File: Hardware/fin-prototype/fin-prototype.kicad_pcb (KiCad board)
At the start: 4 copper layers, 50 x 50 mm, 80 parts, among them J1 USB_C_Receptacle_USB2.0_16P, J10 Conn_01x01_Pin, J11 Conn_01x01_Pin, J12 Conn_01x01_Pin, J13 Conn_01x01_Pin, J14 Conn_01x01_Pin, J15 Conn_01x01_Pin, J16 Conn_01x01_Pin, J17 Conn_01x01_Pin, J18 Conn_01x01_Pin, J2 Conn_01x04_Pin, J3 Conn_01x04_Pin, J4 Conn_01x08_Pin, J5 Conn_01x04_Pin, J6 Conn_01x01_Pin, J7 Conn_01x01_Pin, J8 Conn_01x01_Pin, J9 Conn_01x01_Pin, SW1 SW_Push, SW2 SW_Push, U1 ADS131M03QPWRQ1, U2 STM32L412C8Tx, U3 W25N512GVEIG, U4 TMP235A4DBZR, U5 FT232RNQ-REEL

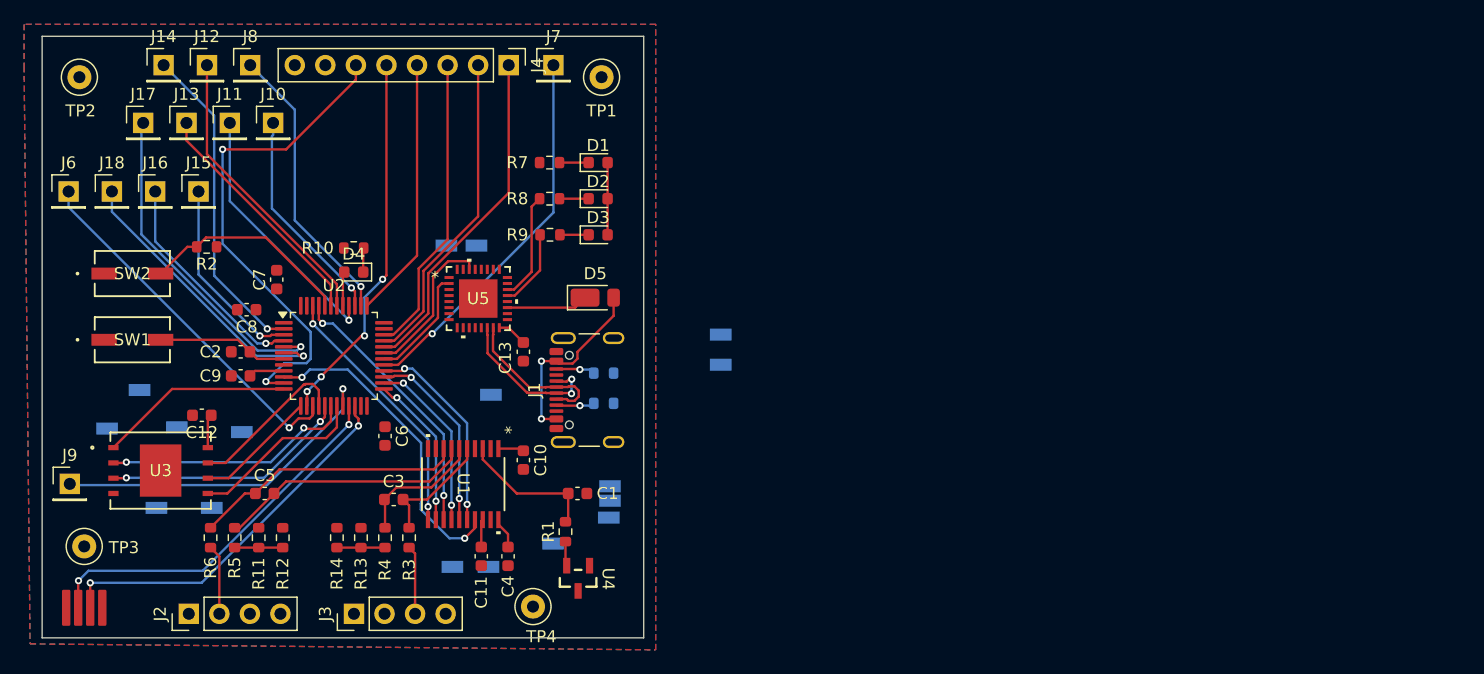
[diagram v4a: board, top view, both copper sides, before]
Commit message: finished routing test points and fixed all build errors
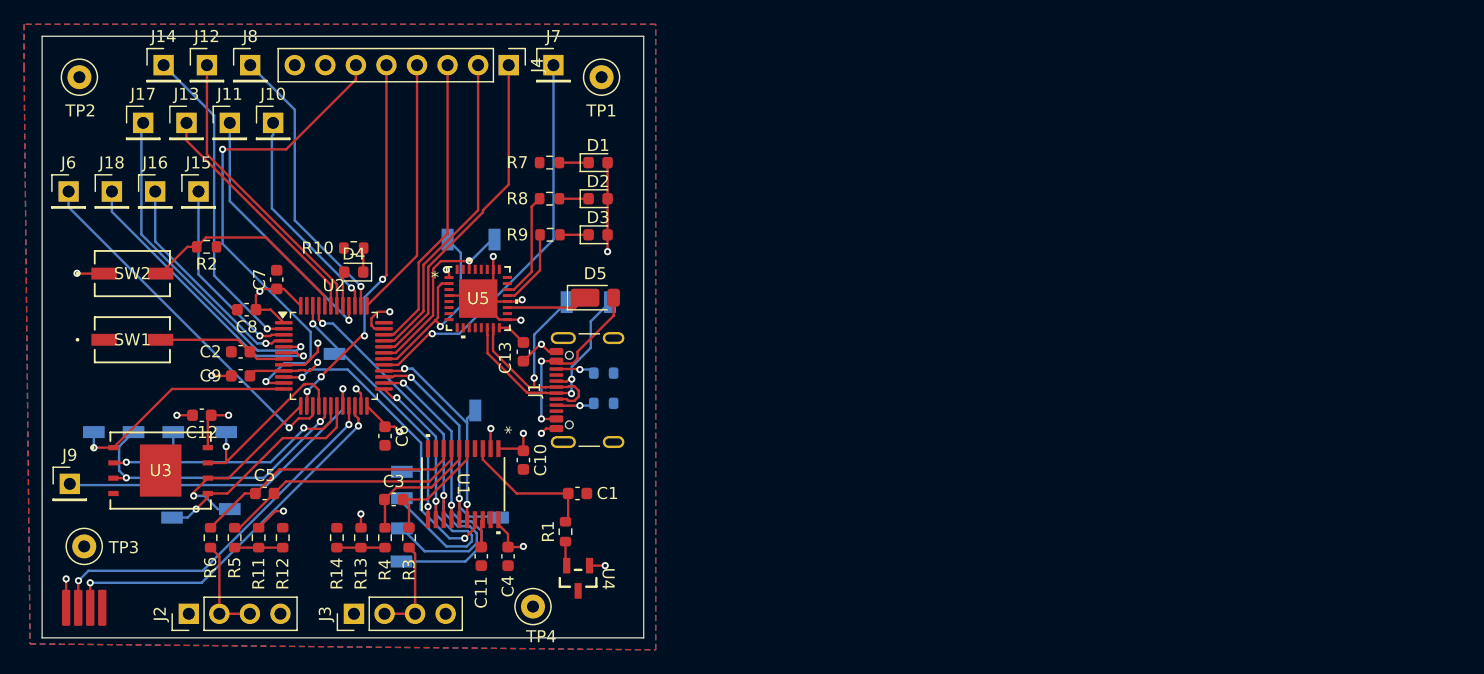
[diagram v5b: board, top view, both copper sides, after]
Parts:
- moved TP10 25.4 mm to (118.8, 70.1)
- moved TP21 18.1 mm to (132.8, 71.1), turned to -90 degrees
- moved TP5 18.1 mm to (124.4, 87.4)
- moved TP20 14.7 mm to (136.4, 71.1), turned to -90 degrees
- moved TP11 12.6 mm to (124.4, 84.6)
- moved TP7 9.28 mm to (125.2, 80.1), turned to -90 degrees
- moved TP6 9.20 mm to (132.4, 94.3)
- moved TP15 9.00 mm to (102.1, 76.6)
- moved TP8 8.71 mm to (124.4, 92.7), turned to 0 degrees
- moved TP19 7.02 mm to (122.9, 65.9), turned to -90 degrees
- moved TP18 6.06 mm to (126.8, 65.9), turned to -90 degrees
- moved TP9 5.00 mm to (124.4, 90.5), turned to 0 degrees
- moved TP14 4.48 mm to (105.4, 76.6)
- moved TP16 4.12 mm to (109.8, 76.6)
- moved TP13 1.53 mm to (105.3, 83.7)
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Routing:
- net GND: track 0.00 -> 33.6 mm, vias 0 -> 11
- net +3.3V: track 16.5 -> 48.1 mm, vias 0 -> 13
- net ~{ADC_CS}: track 12.9 -> 26.0 mm
- net ~{ADC_DRDY}: track 22.6 -> 35.6 mm
- net SPI2_SCK: track 14.6 -> 26.7 mm
- net USART1_TX: track 9.49 -> 18.6 mm, vias 0 -> 1
- net USB_D-: track 13.1 -> 21.3 mm, vias 0 -> 1
- net USB_D+: track 13.1 -> 20.8 mm
- net QSPI_CLK: track 10.2 -> 15.6 mm, vias 0 -> 1
- net QSPI_IO2: track 20.6 -> 25.1 mm
- net SPI2_MISO: track 15.8 -> 20.1 mm
- net QSPI_IO0: track 14.8 -> 18.3 mm, vias 0 -> 1
- net USART1_RX: track 12.8 -> 16.2 mm, vias 0 -> 1
- net ~{FLASH_CS}: track 16.2 -> 18.9 mm, vias 0 -> 1
- net QSPI_IO3: track 13.5 -> 16.1 mm, vias 0 -> 1
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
